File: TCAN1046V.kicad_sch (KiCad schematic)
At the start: 5 parts, among them U5 TCAN1046AVDYYRQ1

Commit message: Start new PCB layout for second test article
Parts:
- renumbered C9 to C13, C10 to C14, C11 to C15, C12 to C16, U5 to U6
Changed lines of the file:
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@@
 		(dnp no)
 		(fields_autoplaced yes)
-		(property "Reference" "U5"
+		(property "Reference" "U6"
 			(at 212.09 118.11 0)
 			(effects
@@
 			(project "HEDGE2-OBC"
 				(path "/a13a6ce3-91ba-42e3-9b40-443fe6a0f2d9/d3868309-a946-47d2-bb65-3f159979e5fb"
-					(reference "U5")
+					(reference "U6")
 					(unit 1)
 				)
@@
 		(dnp no)
 		(fields_autoplaced yes)
-		(property "Reference" "#PWR055"
+		(property "Reference" "#PWR072"
 			(at 179.07 130.81 0)
 			(effects
@@
 			(project "HEDGE2-OBC"
 				(path "/a13a6ce3-91ba-42e3-9b40-443fe6a0f2d9/d3868309-a946-47d2-bb65-3f159979e5fb"
-					(reference "#PWR055")
+					(reference "#PWR072")
 					(unit 1)
 				)
@@
 		(dnp no)
 		(fields_autoplaced yes)
-		(property "Reference" "C12"
+		(property "Reference" "C16"
 			(at 261.62 138.4362 0)
 			(effects
@@
 			(project "HEDGE2-OBC"
 				(path "/a13a6ce3-91ba-42e3-9b40-443fe6a0f2d9/d3868309-a946-47d2-bb65-3f159979e5fb"
-					(reference "C12")
+					(reference "C16")
 					(unit 1)
 				)
@@
 		(dnp no)
 		(fields_autoplaced yes)
-		(property "Reference" "C11"
+		(property "Reference" "C15"
 			(at 252.73 138.4362 0)
 			(effects
@@
 			(project "HEDGE2-OBC"
 				(path "/a13a6ce3-91ba-42e3-9b40-443fe6a0f2d9/d3868309-a946-47d2-bb65-3f159979e5fb"
-					(reference "C11")
+					(reference "C15")
 					(unit 1)
 				)
@@
 		(dnp no)
 		(fields_autoplaced yes)
-		(property "Reference" "#PWR054"
+		(property "Reference" "#PWR071"
 			(at 165.1 151.13 0)
 			(effects
@@
 			(project "HEDGE2-OBC"
 				(path "/a13a6ce3-91ba-42e3-9b40-443fe6a0f2d9/d3868309-a946-47d2-bb65-3f159979e5fb"
-					(reference "#PWR054")
+					(reference "#PWR071")
 					(unit 1)
 				)
@@
 		(dnp no)
 		(fields_autoplaced yes)
-		(property "Reference" "#PWR056"
+		(property "Reference" "#PWR073"
 			(at 179.07 138.43 0)
 			(effects
@@
 			(project "HEDGE2-OBC"
 				(path "/a13a6ce3-91ba-42e3-9b40-443fe6a0f2d9/d3868309-a946-47d2-bb65-3f159979e5fb"
-					(reference "#PWR056")
+					(reference "#PWR073")
 					(unit 1)
 				)
@@
 		(dnp no)
 		(fields_autoplaced yes)
-		(property "Reference" "C9"
+		(property "Reference" "C13"
 			(at 163.83 140.9762 0)
 			(effects
@@
 			(project "HEDGE2-OBC"
 				(path "/a13a6ce3-91ba-42e3-9b40-443fe6a0f2d9/d3868309-a946-47d2-bb65-3f159979e5fb"
-					(reference "C9")
+					(reference "C13")
 					(unit 1)
 				)
@@
 		(dnp no)
 		(fields_autoplaced yes)
-		(property "Reference" "C10"
+		(property "Reference" "C14"
 			(at 172.72 140.9762 0)
 			(effects
@@
 			(project "HEDGE2-OBC"
 				(path "/a13a6ce3-91ba-42e3-9b40-443fe6a0f2d9/d3868309-a946-47d2-bb65-3f159979e5fb"
-					(reference "C10")
+					(reference "C14")
 					(unit 1)
 				)
@@
 		(dnp no)
 		(fields_autoplaced yes)
-		(property "Reference" "#PWR057"
+		(property "Reference" "#PWR074"
 			(at 254 148.59 0)
 			(effects
@@
 			(project "HEDGE2-OBC"
 				(path "/a13a6ce3-91ba-42e3-9b40-443fe6a0f2d9/d3868309-a946-47d2-bb65-3f159979e5fb"
-					(reference "#PWR057")
-					(unit 1)
-				)
+					(reference "#PWR074")
+					(unit 1)
+				)

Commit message: Rework Novatel OEM719B symbol and footprint
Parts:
- renumbered U6 to U7
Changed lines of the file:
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@@
 		(dnp no)
 		(fields_autoplaced yes)
-		(property "Reference" "U6"
+		(property "Reference" "U7"
 			(at 212.09 118.11 0)
 			(effects
@@
 			(project "HEDGE2-OBC"
 				(path "/a13a6ce3-91ba-42e3-9b40-443fe6a0f2d9/d3868309-a946-47d2-bb65-3f159979e5fb"
-					(reference "U6")
+					(reference "U7")
 					(unit 1)
 				)

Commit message: Layout PCB; update footprints with 3D models
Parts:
- renumbered C13 to C15, C14 to C16, C15 to C17, C16 to C18, U7 to U8
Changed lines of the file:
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@@
 		(dnp no)
 		(fields_autoplaced yes)
-		(property "Reference" "U7"
+		(property "Reference" "U8"
 			(at 212.09 118.11 0)
 			(effects
@@
 			(project "HEDGE2-OBC"
 				(path "/a13a6ce3-91ba-42e3-9b40-443fe6a0f2d9/d3868309-a946-47d2-bb65-3f159979e5fb"
-					(reference "U7")
+					(reference "U8")
 					(unit 1)
 				)
@@
 		(dnp no)
 		(fields_autoplaced yes)
-		(property "Reference" "#PWR072"
+		(property "Reference" "#PWR078"
 			(at 179.07 130.81 0)
 			(effects
@@
 			(project "HEDGE2-OBC"
 				(path "/a13a6ce3-91ba-42e3-9b40-443fe6a0f2d9/d3868309-a946-47d2-bb65-3f159979e5fb"
-					(reference "#PWR072")
+					(reference "#PWR078")
 					(unit 1)
 				)
@@
 		(dnp no)
 		(fields_autoplaced yes)
-		(property "Reference" "C16"
+		(property "Reference" "C18"
 			(at 261.62 138.4362 0)
 			(effects
@@
 			(project "HEDGE2-OBC"
 				(path "/a13a6ce3-91ba-42e3-9b40-443fe6a0f2d9/d3868309-a946-47d2-bb65-3f159979e5fb"
-					(reference "C16")
+					(reference "C18")
 					(unit 1)
 				)
@@
 		(dnp no)
 		(fields_autoplaced yes)
-		(property "Reference" "C15"
+		(property "Reference" "C17"
 			(at 252.73 138.4362 0)
 			(effects
@@
 			(project "HEDGE2-OBC"
 				(path "/a13a6ce3-91ba-42e3-9b40-443fe6a0f2d9/d3868309-a946-47d2-bb65-3f159979e5fb"
-					(reference "C15")
+					(reference "C17")
 					(unit 1)
 				)
@@
 		(dnp no)
 		(fields_autoplaced yes)
-		(property "Reference" "#PWR071"
+		(property "Reference" "#PWR077"
 			(at 165.1 151.13 0)
 			(effects
@@
 			(project "HEDGE2-OBC"
 				(path "/a13a6ce3-91ba-42e3-9b40-443fe6a0f2d9/d3868309-a946-47d2-bb65-3f159979e5fb"
-					(reference "#PWR071")
+					(reference "#PWR077")
 					(unit 1)
 				)
@@
 		(dnp no)
 		(fields_autoplaced yes)
-		(property "Reference" "#PWR073"
+		(property "Reference" "#PWR079"
 			(at 179.07 138.43 0)
 			(effects
@@
 			(project "HEDGE2-OBC"
 				(path "/a13a6ce3-91ba-42e3-9b40-443fe6a0f2d9/d3868309-a946-47d2-bb65-3f159979e5fb"
-					(reference "#PWR073")
+					(reference "#PWR079")
 					(unit 1)
 				)
@@
 		(dnp no)
 		(fields_autoplaced yes)
-		(property "Reference" "C13"
+		(property "Reference" "C15"
 			(at 163.83 140.9762 0)
 			(effects
@@
 			(project "HEDGE2-OBC"
 				(path "/a13a6ce3-91ba-42e3-9b40-443fe6a0f2d9/d3868309-a946-47d2-bb65-3f159979e5fb"
-					(reference "C13")
+					(reference "C15")
 					(unit 1)
 				)
@@
 		(dnp no)
 		(fields_autoplaced yes)
-		(property "Reference" "C14"
+		(property "Reference" "C16"
 			(at 172.72 140.9762 0)
 			(effects
@@
 			(project "HEDGE2-OBC"
 				(path "/a13a6ce3-91ba-42e3-9b40-443fe6a0f2d9/d3868309-a946-47d2-bb65-3f159979e5fb"
-					(reference "C14")
+					(reference "C16")
 					(unit 1)
 				)
@@
 		(dnp no)
 		(fields_autoplaced yes)
-		(property "Reference" "#PWR074"
+		(property "Reference" "#PWR080"
 			(at 254 148.59 0)
 			(effects
@@
 			(project "HEDGE2-OBC"
 				(path "/a13a6ce3-91ba-42e3-9b40-443fe6a0f2d9/d3868309-a946-47d2-bb65-3f159979e5fb"
-					(reference "#PWR074")
-					(unit 1)
-				)
+					(reference "#PWR080")
+					(unit 1)
+				)

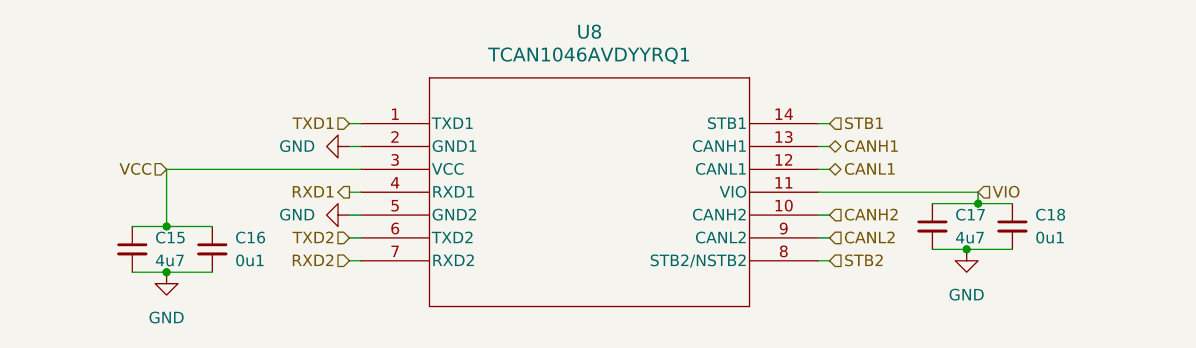
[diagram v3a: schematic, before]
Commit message: Fix MMBX footprint; resolve ERC/DRC
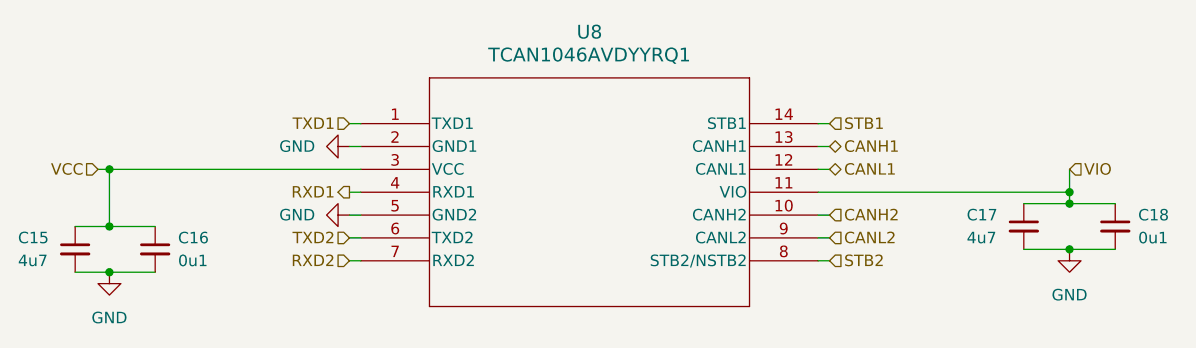
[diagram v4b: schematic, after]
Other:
- moved on the sheet: C15, C16, C17, C18

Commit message: Fix TCAN power supply swap
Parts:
- C15, C17: DigiKey Part Number 720-GA0805Y472KXBBC31GCT-ND -> 490-GRT21BC71H475KE13LCT-ND
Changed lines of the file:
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@@
 			)
 		)
-		(property "DigiKey Part Number" "720-GA0805Y472KXBBC31GCT-ND"
+		(property "DigiKey Part Number" "490-GRT21BC71H475KE13LCT-ND "
 			(at 260.35 139.7 0)
 			(effects
@@
 			)
 		)
-		(property "DigiKey Part Number" "720-GA0805Y472KXBBC31GCT-ND"
-			(at 154.94 142.24 0)
-			(effects
+		(property "DigiKey Part Number" "490-GRT21BC71H475KE13LCT-ND "
+			(at 154.94 142.24 0)
+			(effects

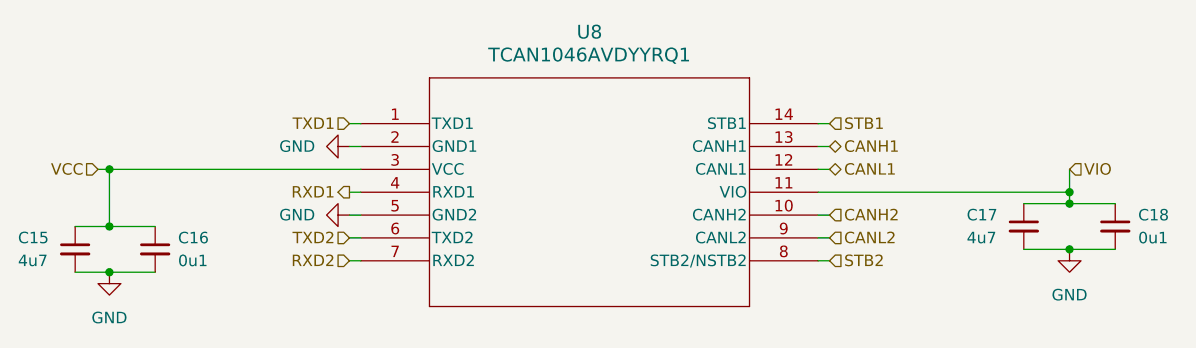
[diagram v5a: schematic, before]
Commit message: Add PCM5102A I2S audio output for APRS radio
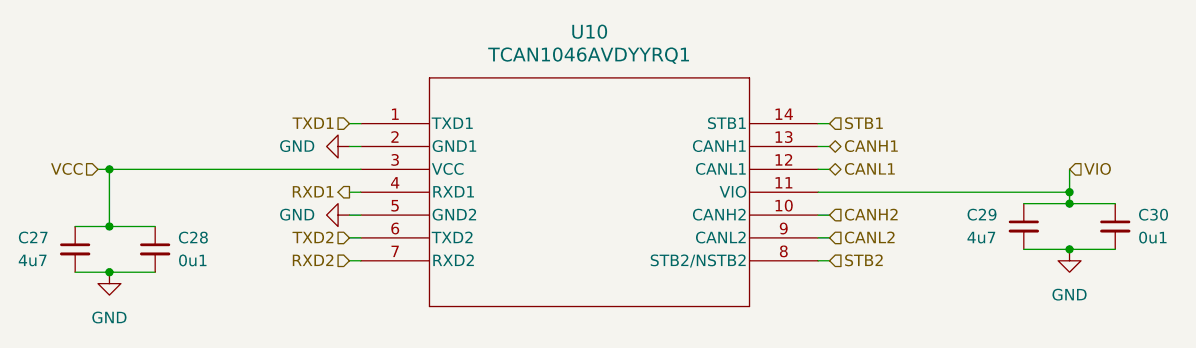
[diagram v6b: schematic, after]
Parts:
- renumbered C15 to C27, C16 to C28, C17 to C29, C18 to C30, U8 to U10
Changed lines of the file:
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@@
 	(generator "eeschema")
 	(generator_version "9.0")
-	(paper "USLedger")
+	(paper "C")
 	(title_block
 		(title "HEDGE-2 OBC")
@@
 		(dnp no)
 		(fields_autoplaced yes)
-		(property "Reference" "U8"
+		(property "Reference" "U10"
 			(at 212.09 118.11 0)
 			(effects
@@
 			)
 		)
-		(property "Datasheet" "https://www.ti.com/lit/gpn/tcan1046av-q1"
+		(property "Datasheet" ""
 			(at 186.69 128.27 0)
 			(effects
@@
 			(project "HEDGE2-OBC"
 				(path "/a13a6ce3-91ba-42e3-9b40-443fe6a0f2d9/d3868309-a946-47d2-bb65-3f159979e5fb"
-					(reference "U8")
+					(reference "U10")
 					(unit 1)
 				)
@@
 		(dnp no)
 		(fields_autoplaced yes)
-		(property "Reference" "#PWR078"
+		(property "Reference" "#PWR092"
 			(at 179.07 130.81 0)
 			(effects
@@
 			(project "HEDGE2-OBC"
 				(path "/a13a6ce3-91ba-42e3-9b40-443fe6a0f2d9/d3868309-a946-47d2-bb65-3f159979e5fb"
-					(reference "#PWR078")
+					(reference "#PWR092")
 					(unit 1)
 				)
@@
 		(dnp no)
 		(fields_autoplaced yes)
-		(property "Reference" "C18"
+		(property "Reference" "C30"
 			(at 273.05 138.4362 0)
 			(effects
@@
 			(project "HEDGE2-OBC"
 				(path "/a13a6ce3-91ba-42e3-9b40-443fe6a0f2d9/d3868309-a946-47d2-bb65-3f159979e5fb"
-					(reference "C18")
+					(reference "C30")
 					(unit 1)
 				)
@@
 		(on_board yes)
 		(dnp no)
-		(property "Reference" "C17"
+		(property "Reference" "C29"
 			(at 254 138.43 0)
 			(effects
@@
 			(project "HEDGE2-OBC"
 				(path "/a13a6ce3-91ba-42e3-9b40-443fe6a0f2d9/d3868309-a946-47d2-bb65-3f159979e5fb"
-					(reference "C17")
+					(reference "C29")
 					(unit 1)
 				)
@@
 		(dnp no)
 		(fields_autoplaced yes)
-		(property "Reference" "#PWR077"
+		(property "Reference" "#PWR089"
 			(at 158.75 151.13 0)
 			(effects
@@
 			(project "HEDGE2-OBC"
 				(path "/a13a6ce3-91ba-42e3-9b40-443fe6a0f2d9/d3868309-a946-47d2-bb65-3f159979e5fb"
-					(reference "#PWR077")
+					(reference "#PWR089")
 					(unit 1)
 				)
@@
 		(dnp no)
 		(fields_autoplaced yes)
-		(property "Reference" "#PWR079"
+		(property "Reference" "#PWR093"
 			(at 179.07 138.43 0)
 			(effects
@@
 			(project "HEDGE2-OBC"
 				(path "/a13a6ce3-91ba-42e3-9b40-443fe6a0f2d9/d3868309-a946-47d2-bb65-3f159979e5fb"
-					(reference "#PWR079")
+					(reference "#PWR093")
 					(unit 1)
 				)
@@
 		(on_board yes)
 		(dnp no)
-		(property "Reference" "C15"
+		(property "Reference" "C27"
 			(at 148.59 140.97 0)
 			(effects
@@
 			(project "HEDGE2-OBC"
 				(path "/a13a6ce3-91ba-42e3-9b40-443fe6a0f2d9/d3868309-a946-47d2-bb65-3f159979e5fb"
-					(reference "C15")
+					(reference "C27")
 					(unit 1)
 				)
@@
 		(dnp no)
 		(fields_autoplaced yes)
-		(property "Reference" "C16"
+		(property "Reference" "C28"
 			(at 166.37 140.9762 0)
 			(effects
@@
 			(project "HEDGE2-OBC"
 				(path "/a13a6ce3-91ba-42e3-9b40-443fe6a0f2d9/d3868309-a946-47d2-bb65-3f159979e5fb"
-					(reference "C16")
+					(reference "C28")
 					(unit 1)
 				)
@@
 		(dnp no)
 		(fields_autoplaced yes)
-		(property "Reference" "#PWR080"
+		(property "Reference" "#PWR094"
 			(at 265.43 148.59 0)
 			(effects
@@
 			(project "HEDGE2-OBC"
 				(path "/a13a6ce3-91ba-42e3-9b40-443fe6a0f2d9/d3868309-a946-47d2-bb65-3f159979e5fb"
-					(reference "#PWR080")
+					(reference "#PWR094")
 					(unit 1)
 				)

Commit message: Add PCM and SPI UART; begin layout update
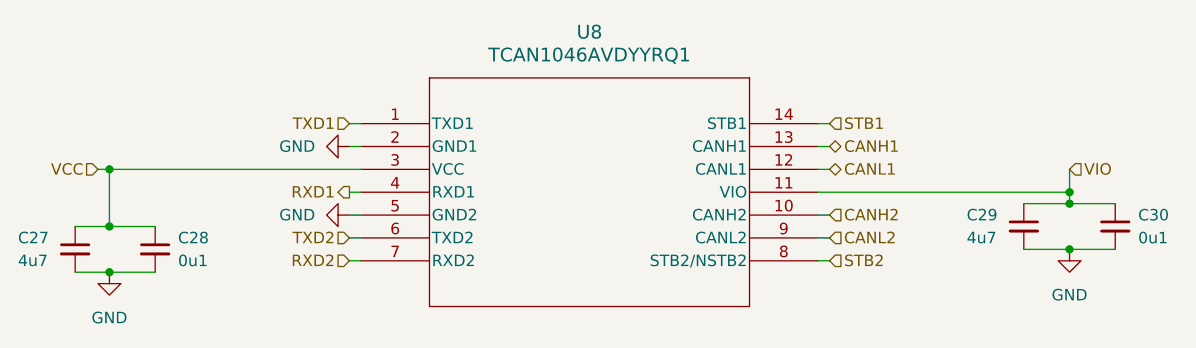
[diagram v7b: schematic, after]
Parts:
- renumbered U10 to U8
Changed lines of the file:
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@@
 		(dnp no)
 		(fields_autoplaced yes)
-		(property "Reference" "U10"
+		(property "Reference" "U8"
 			(at 212.09 118.11 0)
 			(effects
@@
 			(project "HEDGE2-OBC"
 				(path "/a13a6ce3-91ba-42e3-9b40-443fe6a0f2d9/d3868309-a946-47d2-bb65-3f159979e5fb"
-					(reference "U10")
+					(reference "U8")
 					(unit 1)
 				)
@@
 		(dnp no)
 		(fields_autoplaced yes)
-		(property "Reference" "#PWR092"
+		(property "Reference" "#PWR088"
 			(at 179.07 130.81 0)
 			(effects
@@
 			(project "HEDGE2-OBC"
 				(path "/a13a6ce3-91ba-42e3-9b40-443fe6a0f2d9/d3868309-a946-47d2-bb65-3f159979e5fb"
-					(reference "#PWR092")
+					(reference "#PWR088")
 					(unit 1)
 				)
@@
 		(dnp no)
 		(fields_autoplaced yes)
-		(property "Reference" "#PWR089"
+		(property "Reference" "#PWR087"
 			(at 158.75 151.13 0)
 			(effects
@@
 			(project "HEDGE2-OBC"
 				(path "/a13a6ce3-91ba-42e3-9b40-443fe6a0f2d9/d3868309-a946-47d2-bb65-3f159979e5fb"
-					(reference "#PWR089")
+					(reference "#PWR087")
 					(unit 1)
 				)
@@
 		(dnp no)
 		(fields_autoplaced yes)
-		(property "Reference" "#PWR093"
+		(property "Reference" "#PWR089"
 			(at 179.07 138.43 0)
 			(effects
@@
 			(project "HEDGE2-OBC"
 				(path "/a13a6ce3-91ba-42e3-9b40-443fe6a0f2d9/d3868309-a946-47d2-bb65-3f159979e5fb"
-					(reference "#PWR093")
+					(reference "#PWR089")
 					(unit 1)
 				)
@@
 		(dnp no)
 		(fields_autoplaced yes)
-		(property "Reference" "#PWR094"
+		(property "Reference" "#PWR090"
 			(at 265.43 148.59 0)
 			(effects
@@
 			(project "HEDGE2-OBC"
 				(path "/a13a6ce3-91ba-42e3-9b40-443fe6a0f2d9/d3868309-a946-47d2-bb65-3f159979e5fb"
-					(reference "#PWR094")
-					(unit 1)
-				)
+					(reference "#PWR090")
+					(unit 1)
+				)

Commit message: Continue layout update
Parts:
- renumbered C27 to C26, C28 to C27, C29 to C28, C30 to C29
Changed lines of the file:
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@@
 		(dnp no)
 		(fields_autoplaced yes)
-		(property "Reference" "#PWR088"
+		(property "Reference" "#PWR094"
 			(at 179.07 130.81 0)
 			(effects
@@
 			(project "HEDGE2-OBC"
 				(path "/a13a6ce3-91ba-42e3-9b40-443fe6a0f2d9/d3868309-a946-47d2-bb65-3f159979e5fb"
-					(reference "#PWR088")
+					(reference "#PWR094")
 					(unit 1)
 				)
@@
 		(dnp no)
 		(fields_autoplaced yes)
-		(property "Reference" "C30"
+		(property "Reference" "C29"
 			(at 273.05 138.4362 0)
 			(effects
@@
 			(project "HEDGE2-OBC"
 				(path "/a13a6ce3-91ba-42e3-9b40-443fe6a0f2d9/d3868309-a946-47d2-bb65-3f159979e5fb"
-					(reference "C30")
+					(reference "C29")
 					(unit 1)
 				)
@@
 		(on_board yes)
 		(dnp no)
-		(property "Reference" "C29"
+		(property "Reference" "C28"
 			(at 254 138.43 0)
 			(effects
@@
 			(project "HEDGE2-OBC"
 				(path "/a13a6ce3-91ba-42e3-9b40-443fe6a0f2d9/d3868309-a946-47d2-bb65-3f159979e5fb"
-					(reference "C29")
+					(reference "C28")
 					(unit 1)
 				)
@@
 		(dnp no)
 		(fields_autoplaced yes)
-		(property "Reference" "#PWR087"
+		(property "Reference" "#PWR093"
 			(at 158.75 151.13 0)
 			(effects
@@
 			(project "HEDGE2-OBC"
 				(path "/a13a6ce3-91ba-42e3-9b40-443fe6a0f2d9/d3868309-a946-47d2-bb65-3f159979e5fb"
-					(reference "#PWR087")
+					(reference "#PWR093")
 					(unit 1)
 				)
@@
 		(dnp no)
 		(fields_autoplaced yes)
-		(property "Reference" "#PWR089"
+		(property "Reference" "#PWR095"
 			(at 179.07 138.43 0)
 			(effects
@@
 			(project "HEDGE2-OBC"
 				(path "/a13a6ce3-91ba-42e3-9b40-443fe6a0f2d9/d3868309-a946-47d2-bb65-3f159979e5fb"
-					(reference "#PWR089")
+					(reference "#PWR095")
 					(unit 1)
 				)
@@
 		(on_board yes)
 		(dnp no)
-		(property "Reference" "C27"
+		(property "Reference" "C26"
 			(at 148.59 140.97 0)
 			(effects
@@
 			(project "HEDGE2-OBC"
 				(path "/a13a6ce3-91ba-42e3-9b40-443fe6a0f2d9/d3868309-a946-47d2-bb65-3f159979e5fb"
-					(reference "C27")
+					(reference "C26")
 					(unit 1)
 				)
@@
 		(dnp no)
 		(fields_autoplaced yes)
-		(property "Reference" "C28"
+		(property "Reference" "C27"
 			(at 166.37 140.9762 0)
 			(effects
@@
 			(project "HEDGE2-OBC"
 				(path "/a13a6ce3-91ba-42e3-9b40-443fe6a0f2d9/d3868309-a946-47d2-bb65-3f159979e5fb"
-					(reference "C28")
+					(reference "C27")
 					(unit 1)
 				)
@@
 		(dnp no)
 		(fields_autoplaced yes)
-		(property "Reference" "#PWR090"
+		(property "Reference" "#PWR096"
 			(at 265.43 148.59 0)
 			(effects
@@
 			(project "HEDGE2-OBC"
 				(path "/a13a6ce3-91ba-42e3-9b40-443fe6a0f2d9/d3868309-a946-47d2-bb65-3f159979e5fb"
-					(reference "#PWR090")
-					(unit 1)
-				)
+					(reference "#PWR096")
+					(unit 1)
+				)
